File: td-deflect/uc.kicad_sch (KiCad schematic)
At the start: 18 parts, among them J4 Conn_ARM_JTAG_SWD_10, J6 Conn_01x06_Male, U12 LM1117-5.0, U2 STM32F722RETx, U3 INA193, U4 TPS70933, X1 SG-8002CA

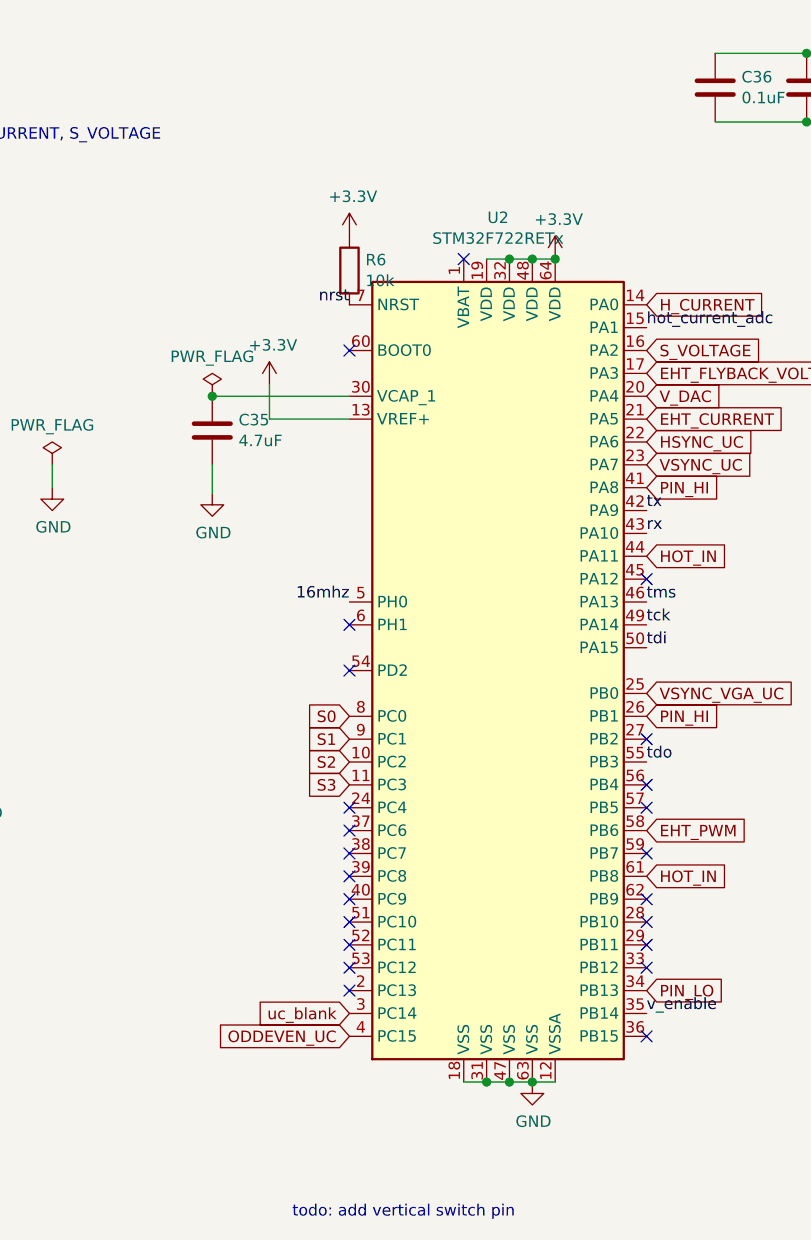
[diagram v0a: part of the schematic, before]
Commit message: switch to stm32g4
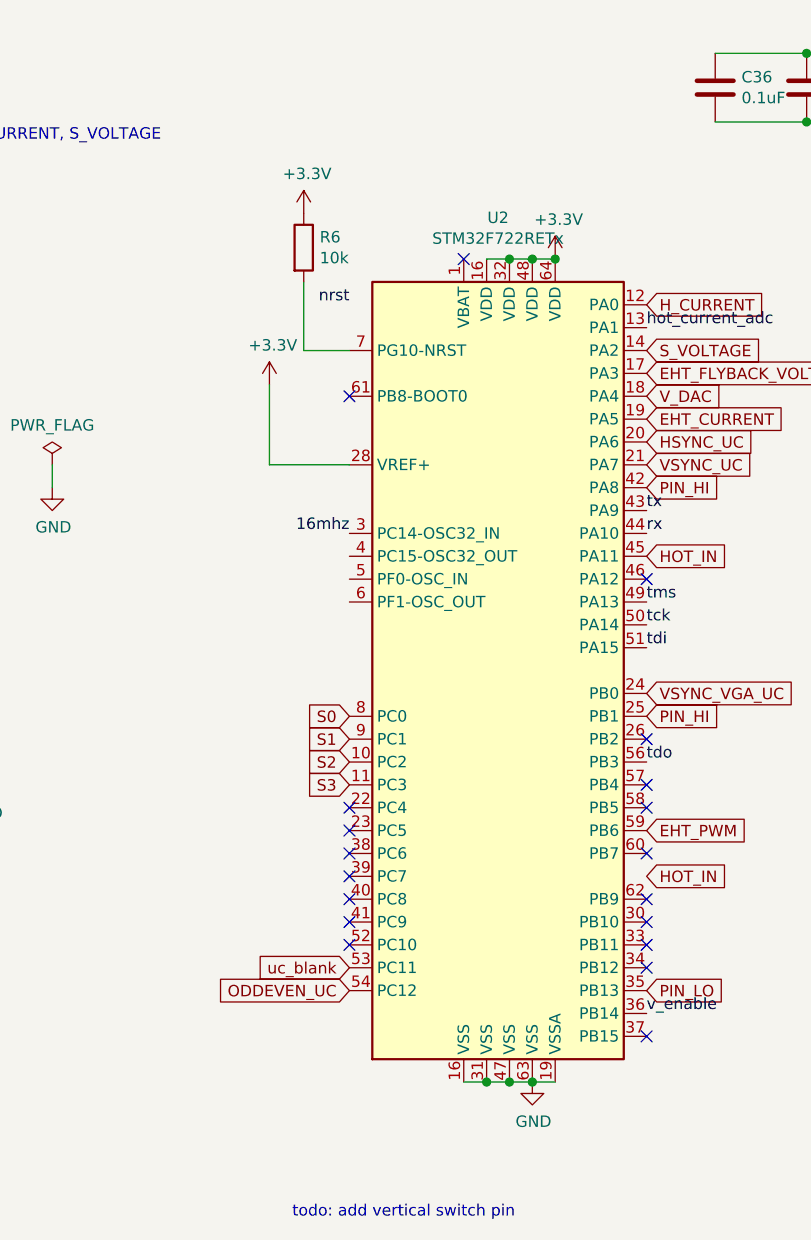
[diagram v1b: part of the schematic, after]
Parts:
- removed C35: 4.7uF, Capacitor_SMD:C_0805_2012Metric_Pad1.15x1.40mm_HandSolder, symbol Device:C
- U2: symbol MCU_ST_STM32F7:STM32F722RETx -> td-crt:STM32G474xx
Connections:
- net +3V3: now also U2.16 (VSS), U2.28 (VREF+); no longer U2.13 (VREF+), U2.19 (VDD)
- net 16mhz: now also U2.3 (PC14-OSC32_IN); no longer U2.5 (PH0)
- net EHT_CURRENT: now also U2.19 (VSSA); no longer U2.21 (PA5)
- net EHT_PWM: now also U2.59 (PB6); no longer U2.58 (PB6)
- net GND: now also U2.16 (VSS), U2.19 (VSSA); no longer U2.12 (VSSA), U2.18 (VSS)
- net HOT_IN: now also U2.45 (PA11); no longer U2.44 (PA11), U2.61 (PB8)
- net HSYNC_UC: now also U2.20 (PA6); no longer U2.22 (PA6)
- net H_CURRENT: now also U2.12 (PA0); no longer U2.14 (PA0)
- net ODDEVEN_UC: now also U2.54 (PC12); no longer U2.4 (PC15)
- net PIN_HI: now also U2.25 (PB1), U2.42 (PA8); no longer U2.26 (PB1), U2.41 (PA8)
- net PIN_LO: now also U2.35 (PB13); no longer U2.34 (PB13)
- net S_VOLTAGE: now also U2.14 (PA2); no longer U2.16 (PA2)
- net VSYNC_UC: now also U2.21 (PA7); no longer U2.23 (PA7)
- net VSYNC_VGA_UC: now also U2.24 (PB0); no longer U2.25 (PB0)
- net V_DAC: now also U2.18 (PA4); no longer U2.20 (PA4)
- net hot_current_adc: now also U2.13 (PA1); no longer U2.15 (PA1)
- net nrst: no longer R6.2, U2.7 (NRST)
- net rx: now also U2.44 (PA10); no longer U2.43 (PA10)
- net tck: now also U2.50 (PA14); no longer U2.49 (PA14)
- net tdi: now also U2.51 (PA15); no longer U2.50 (PA15)
- net tdo: now also U2.56 (PB3); no longer U2.55 (PB3)
- net tms: now also U2.49 (PA13); no longer U2.46 (PA13)
- net tx: now also U2.43 (PA9); no longer U2.42 (PA9)
- net uc_blank: now also U2.53 (PC11); no longer U2.3 (PC14)
- net v_enable: now also U2.36 (PB14); no longer U2.35 (PB14)
- new net: R6.2, U2.7 (PG10-NRST)
- no-connect marks 26 -> 22
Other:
- moved on the sheet: R6
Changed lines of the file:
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@@
   (junction (at 161.29 21.59) (diameter 1.016) (color 0 0 0 0)
-  )
-  (junction (at 85.09 59.69) (diameter 1.016) (color 0 0 0 0)
   )
   (junction (at 115.57 135.89) (diameter 1.016) (color 0 0 0 0)
@@
   (no_connect (at 100.33 113.03))
   (no_connect (at 50.8 104.14))
-  (no_connect (at 100.33 125.73))
   (no_connect (at 133.35 130.81))
   (no_connect (at 133.35 97.79))
@@
   (no_connect (at 100.33 120.65))
   (no_connect (at 133.35 105.41))
-  (no_connect (at 100.33 123.19))
+  (no_connect (at 100.33 59.69))
   (no_connect (at 133.35 115.57))
   (no_connect (at 100.33 115.57))
   (no_connect (at 133.35 80.01))
   (no_connect (at 100.33 118.11))
-  (no_connect (at 100.33 54.61))
-  (no_connect (at 100.33 90.17))
-  (no_connect (at 100.33 85.09))
   (no_connect (at 100.33 105.41))
   (no_connect (at 133.35 120.65))
@@
     (stroke (width 0) (type solid) (color 0 0 0 0))
   )
-  (wire (pts (xy 91.44 62.23) (xy 91.44 58.42))
-    (stroke (width 0) (type solid) (color 0 0 0 0))
+  (wire (pts (xy 91.44 58.42) (xy 91.44 67.31))
+    (stroke (width 0) (type solid) (color 0 0 0 0))
+  )
+  (wire (pts (xy 95.25 54.61) (xy 95.25 46.99))
+    (stroke (width 0) (type default) (color 0 0 0 0))
   )
   (wire (pts (xy 181.61 129.54) (xy 181.61 134.62))
     (stroke (width 0) (type solid) (color 0 0 0 0))
   )
-  (wire (pts (xy 100.33 62.23) (xy 91.44 62.23))
-    (stroke (width 0) (type solid) (color 0 0 0 0))
-  )
-  (wire (pts (xy 85.09 59.69) (xy 100.33 59.69))
-    (stroke (width 0) (type solid) (color 0 0 0 0))
-  )
   (wire (pts (xy 224.79 83.82) (xy 217.17 83.82))
     (stroke (width 0) (type solid) (color 0 0 0 0))
@@
     (stroke (width 0) (type solid) (color 0 0 0 0))
   )
-  (wire (pts (xy 85.09 67.31) (xy 85.09 70.485))
-    (stroke (width 0) (type solid) (color 0 0 0 0))
-  )
   (wire (pts (xy 217.17 83.82) (xy 217.17 91.44))
     (stroke (width 0) (type solid) (color 0 0 0 0))
@@
     (stroke (width 0) (type solid) (color 0 0 0 0))
   )
+  (wire (pts (xy 100.33 67.31) (xy 91.44 67.31))
+    (stroke (width 0) (type default) (color 0 0 0 0))
+  )
   (wire (pts (xy 120.65 44.45) (xy 123.19 44.45))
     (stroke (width 0) (type solid) (color 0 0 0 0))
@@
   (wire (pts (xy 123.19 135.89) (xy 120.65 135.89))
     (stroke (width 0) (type solid) (color 0 0 0 0))
+  )
+  (wire (pts (xy 100.33 54.61) (xy 95.25 54.61))
+    (stroke (width 0) (type default) (color 0 0 0 0))
   )
   (text "Peripheral assignments:\nADC0 - HOT_CURRENT, H_CURRENT, S_VOLTAGE\nTIM3 - hsync, vsync\nTIM10 - HOT_IN"
@@
     (effects (font (size 1.27 1.27)) (justify right bottom))
   )
-  (label "16mhz" (at 100.33 82.55 180)
+  (label "16mhz" (at 100.33 74.93 180)
     (effects (font (size 1.27 1.27)) (justify right bottom))
   )
@@
     )
   )
-  (global_label "uc_blank" (shape input) (at 100.33 128.27 180) (fields_autoplaced)
+  (global_label "uc_blank" (shape input) (at 100.33 123.19 180) (fields_autoplaced)
     (effects (font (size 1.27 1.27)) (justify right))
-    (property "Intersheet References" "${INTERSHEET_REFS}" (id 0) (at 0 0 0)
+    (property "Intersheet References" "${INTERSHEET_REFS}" (id 0) (at 0 -5.08 0)
       (effects (font (size 1.27 1.27)) hide)
     )
@@
     )
   )
-  (global_label "ODDEVEN_UC" (shape input) (at 100.33 130.81 180) (fields_autoplaced)
+  (global_label "ODDEVEN_UC" (shape input) (at 100.33 125.73 180) (fields_autoplaced)
     (effects (font (size 1.27 1.27)) (justify right))
-    (property "Intersheet References" "${INTERSHEET_REFS}" (id 0) (at 0 0 0)
+    (property "Intersheet References" "${INTERSHEET_REFS}" (id 0) (at 0 -5.08 0)
       (effects (font (size 1.27 1.27)) hide)
     )
@@
     (pin "1")
   )
-  (symbol (lib_id "MCU_ST_STM32F7:STM32F722RETx") (at 118.11 90.17 0) (unit 1)
+  (symbol (lib_id "td-crt:STM32G474xx") (at 118.11 90.17 0) (unit 1)
     (in_bom yes) (on_board yes)
     (property "Reference" "U2" (id 0) (at 116.84 39.8526 0))
@@
       (effects (font (size 1.27 1.27)) (justify right) hide)
     )
-    (property "Datasheet" "http://www.st.com/st-web-ui/static/active/en/resource/technical/document/datasheet/DM00330506.pdf" (id 3) (at 118.11 90.17 0)
+    (property "Datasheet" "https://www.st.com/resource/en/datasheet/stm32g474cb.pdf" (id 3) (at 118.11 90.17 0)
       (effects (font (size 1.27 1.27)) hide)
     )
@@
     (pin "13")
     (pin "14")
-    (pin "15")
+    (pin "16")
     (pin "16")
     (pin "17")
     (pin "18")
     (pin "19")
-    (pin "2")
+    (pin "19")
     (pin "20")
     (pin "21")
@@
     (pin "25")
     (pin "26")
-    (pin "27")
     (pin "28")
-    (pin "29")
     (pin "3")
     (pin "30")
@@
     (pin "53")
     (pin "54")
-    (pin "55")
     (pin "56")
     (pin "57")
@@
     (pin "1")
   )
-  (symbol (lib_id "Device:R") (at 100.33 45.72 0) (unit 1)
-    (in_bom yes) (on_board yes)
-    (property "Reference" "R6" (id 0) (at 102.108 44.5516 0)
-      (effects (font (size 1.27 1.27)) (justify left))
-    )
-    (property "Value" "10k" (id 1) (at 102.108 46.863 0)
-      (effects (font (size 1.27 1.27)) (justify left))
-    )
-    (property "Footprint" "Resistor_SMD:R_0805_2012Metric_Pad1.15x1.40mm_HandSolder" (id 2) (at 98.552 45.72 90)
-      (effects (font (size 1.27 1.27)) hide)
-    )
-    (property "Datasheet" "~" (id 3) (at 100.33 45.72 0)
-      (effects (font (size 1.27 1.27)) hide)
-    )
-    (property "Digikey" "" (id 4) (at 100.33 45.72 0)
-      (effects (font (size 1.27 1.27)) hide)
-    )
-    (pin "1")
-    (pin "2")
-  )
-  (symbol (lib_id "power:+3.3V") (at 100.33 41.91 0) (unit 1)
-    (in_bom yes) (on_board yes)
-    (property "Reference" "#PWR0132" (id 0) (at 100.33 45.72 0)
-      (effects (font (size 1.27 1.27)) hide)
-    )
-    (property "Value" "+3.3V" (id 1) (at 100.711 37.5158 0))
-    (property "Footprint" "" (id 2) (at 100.33 41.91 0)
-      (effects (font (size 1.27 1.27)) hide)
-    )
-    (property "Datasheet" "" (id 3) (at 100.33 41.91 0)
+  (symbol (lib_id "Device:R") (at 95.25 43.18 0) (unit 1)
+    (in_bom yes) (on_board yes)
+    (property "Reference" "R6" (id 0) (at 97.028 42.0116 0)
+      (effects (font (size 1.27 1.27)) (justify left))
+    )
+    (property "Value" "10k" (id 1) (at 97.028 44.323 0)
+      (effects (font (size 1.27 1.27)) (justify left))
+    )
+    (property "Footprint" "Resistor_SMD:R_0805_2012Metric_Pad1.15x1.40mm_HandSolder" (id 2) (at 93.472 43.18 90)
+      (effects (font (size 1.27 1.27)) hide)
+    )
+    (property "Datasheet" "~" (id 3) (at 95.25 43.18 0)
+      (effects (font (size 1.27 1.27)) hide)
+    )
+    (property "Digikey" "" (id 4) (at 95.25 43.18 0)
+      (effects (font (size 1.27 1.27)) hide)
+    )
+    (pin "1")
+    (pin "2")
+  )
+  (symbol (lib_id "power:+3.3V") (at 95.25 39.37 0) (unit 1)
+    (in_bom yes) (on_board yes)
+    (property "Reference" "#PWR0132" (id 0) (at 95.25 43.18 0)
+      (effects (font (size 1.27 1.27)) hide)
+    )
+    (property "Value" "+3.3V" (id 1) (at 95.631 34.9758 0))
+    (property "Footprint" "" (id 2) (at 95.25 39.37 0)
+      (effects (font (size 1.27 1.27)) hide)
+    )
+    (property "Datasheet" "" (id 3) (at 95.25 39.37 0)
       (effects (font (size 1.27 1.27)) hide)
     )
@@
     (pin "1")
     (pin "2")
-  )
-  (symbol (lib_id "Device:C") (at 85.09 63.5 0) (unit 1)
-    (in_bom yes) (on_board yes)
-    (property "Reference" "C35" (id 0) (at 88.011 62.3316 0)
-      (effects (font (size 1.27 1.27)) (justify left))
-    )
-    (property "Value" "4.7uF" (id 1) (at 88.011 64.643 0)
-      (effects (font (size 1.27 1.27)) (justify left))
-    )
-    (property "Footprint" "Capacitor_SMD:C_0805_2012Metric_Pad1.15x1.40mm_HandSolder" (id 2) (at 86.0552 67.31 0)
-      (effects (font (size 1.27 1.27)) hide)
-    )
-    (property "Datasheet" "~" (id 3) (at 85.09 63.5 0)
-      (effects (font (size 1.27 1.27)) hide)
-    )
-    (property "Voltage" "10V" (id 4) (at 85.09 63.5 0)
-      (effects (font (size 1.27 1.27)) hide)
-    )
-    (property "Digikey" "1276-3177-1-ND" (id 5) (at 85.09 63.5 0)
-      (effects (font (size 1.27 1.27)) hide)
-    )
-    (pin "1")
-    (pin "2")
-  )
-  (symbol (lib_id "power:GND") (at 85.09 70.485 0) (unit 1)
-    (in_bom yes) (on_board yes)
-    (property "Reference" "#PWR0139" (id 0) (at 85.09 76.835 0)
-      (effects (font (size 1.27 1.27)) hide)
-    )
-    (property "Value" "GND" (id 1) (at 85.217 74.8792 0))
-    (property "Footprint" "" (id 2) (at 85.09 70.485 0)
-      (effects (font (size 1.27 1.27)) hide)
-    )
-    (property "Datasheet" "" (id 3) (at 85.09 70.485 0)
-      (effects (font (size 1.27 1.27)) hide)
-    )
-    (pin "1")
   )
   (symbol (lib_id "Device:C") (at 208.28 34.29 0) (unit 1)
@@
       (effects (font (size 1.27 1.27)) hide)
     )
-    (pin "1")
-  )
-  (symbol (lib_id "power:PWR_FLAG") (at 85.09 59.69 0) (unit 1)
-    (in_bom yes) (on_board yes)
-    (property "Reference" "#FLG0105" (id 0) (at 85.09 57.785 0)
-      (effects (font (size 1.27 1.27)) hide)
-    )
-    (property "Value" "PWR_FLAG" (id 1) (at 85.09 55.2958 0))
-    (property "Footprint" "" (id 2) (at 85.09 59.69 0)
-      (effects (font (size 1.27 1.27)) hide)
-    )
-    (property "Datasheet" "~" (id 3) (at 85.09 59.69 0)
-      (effects (font (size 1.27 1.27)) hide)
-    )

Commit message: current measurement for h
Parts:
- U2: value STM32F722RETx -> STM32G474xx; Digikey 497-17184-ND -> (none)
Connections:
- net nrst: now also R6.2, U2.7 (PG10-NRST)
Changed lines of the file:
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@@
     (effects (font (size 1.27 1.27)) (justify left bottom))
   )
-  (label "nrst" (at 100.33 49.53 180)
+  (label "nrst" (at 99.06 54.61 180)
     (effects (font (size 1.27 1.27)) (justify right bottom))
   )
@@
     (in_bom yes) (on_board yes)
     (property "Reference" "U2" (id 0) (at 116.84 39.8526 0))
-    (property "Value" "STM32F722RETx" (id 1) (at 116.84 42.164 0))
+    (property "Value" "STM32G474xx" (id 1) (at 116.84 42.164 0))
     (property "Footprint" "Package_QFP:LQFP-64_10x10mm_P0.5mm" (id 2) (at 102.87 133.35 0)
       (effects (font (size 1.27 1.27)) (justify right) hide)
@@
       (effects (font (size 1.27 1.27)) hide)
     )
-    (property "Digikey" "497-17184-ND" (id 4) (at 118.11 90.17 0)
-      (effects (font (size 1.27 1.27)) hide)
-    )
+    (property "Digikey" "" (id 4) (at 118.11 90.17 0)
+      (effects (font (size 1.27 1.27)) hide)
+    )
